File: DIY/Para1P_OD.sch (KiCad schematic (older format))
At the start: 5 parts, among them J1 Atari_SEGA_DE9, J2 DB25_Male, U1 74AHCT125N, U2 74AHCT125N, U3 74AHCT125N

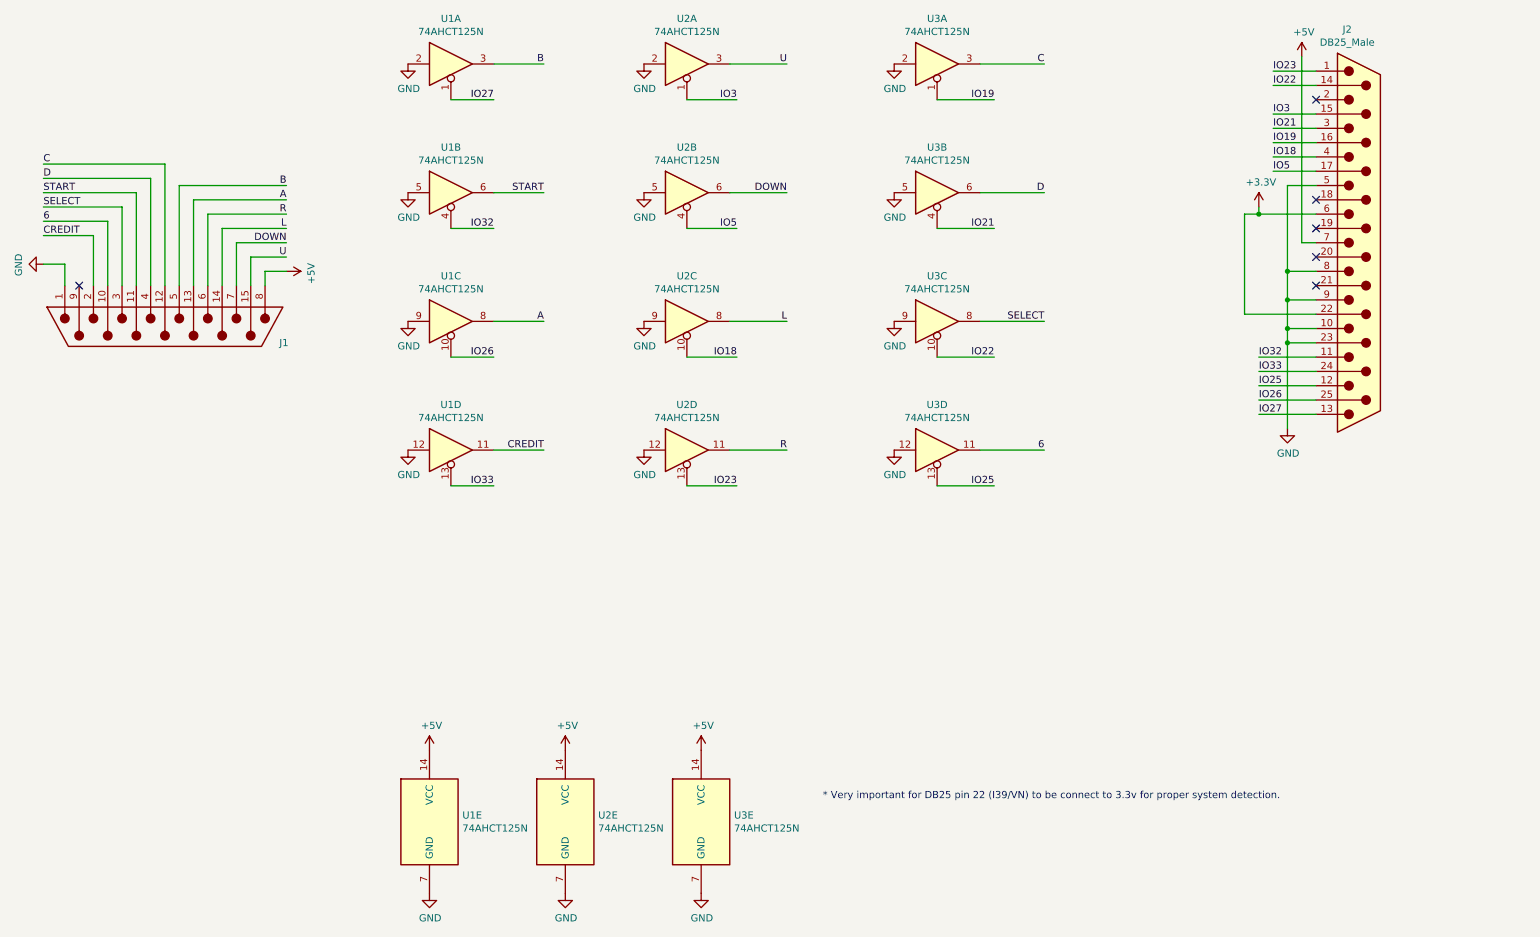
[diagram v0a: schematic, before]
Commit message: Simplify parallel schematics
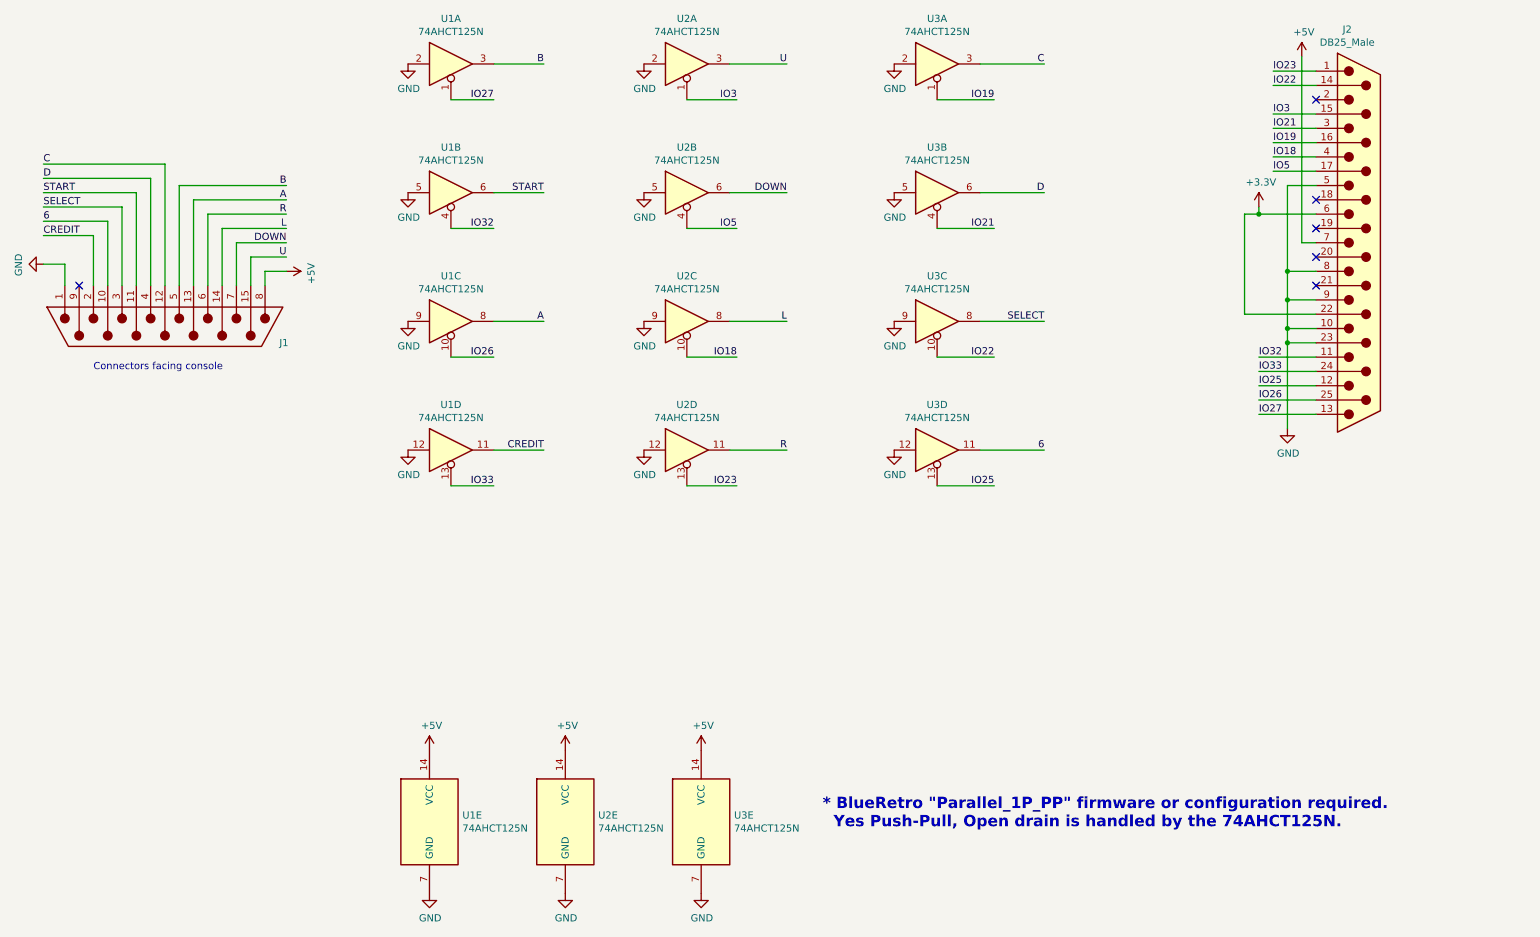
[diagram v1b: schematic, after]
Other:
- note added: "* BlueRetro "Parallel_1P_PP" firmware or configuration required.\n Yes Push-Pull, Open drain is handled by the 74AHCT125N."
- note added: "Connectors facing console"
- note removed: "* Very important for DB25 pin 22 (I39/VN) to be connect to 3.3v for proper system detection."
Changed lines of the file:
@@
 $Descr USLetter 11000 8500
 encoding utf-8
-Sheet 19 19
+Sheet 19 20
 Title "BlueRetro - Parallel 1P Open Drain adapter cable"
 Date "2022-01-30"
 Rev "v1.0"
-Comp "©2022 Jacques Gagnon, licensed under CC-BY-4.0"
+Comp "©2020-2022 Jacques Gagnon, licensed under CC-BY-4.0"
 Comment1 ""
 Comment2 ""
@@
 	1    0    0    -1
 $EndComp
-Text Notes 6350 6900 0    50   ~ 0
-* Very important for DB25 pin 22 (I39/VN) to be connect to 3.3v for proper system detection.
 $Comp
 L power:GND #PWR?
@@
 Wire Wire Line
 	3750 2000 4050 2000
+Text Notes 1250 3900 0    50   ~ 0
+Connectors facing console
+Text Notes 6350 7100 0    79   ~ 16
+* BlueRetro "Parallel_1P_PP" firmware or configuration required.\n  Yes Push-Pull, Open drain is handled by the 74AHCT125N.
 $EndSCHEMATC
